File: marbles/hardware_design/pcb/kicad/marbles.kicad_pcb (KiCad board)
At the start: 2 copper layers, 88.9 x 106 mm, 213 parts, among them IC1 R-78E3.3-0.5, IC10 TL074PW, IC2 STM32F405RGT6, IC3 LD2981ABU33, IC4 DAC8164ICPW, IC5 MCP6004, IC6 MCP6004, IC7 OPA4171, IC8 LM4040B10, IC9 LM324PW, J1 PJ301_THONKICONN6, J10 PJ301_THONKICONN6, J11 PJ301_THONKICONN6, J12 PJ301_THONKICONN6, J13 PJ301_THONKICONN6, J14 PJ301_THONKICONN6, J15 PJ301_THONKICONN6, J16 PJ301_THONKICONN6, J2 PJ301_THONKICONN6, J3 PJ301_THONKICONN6, J4 PJ301_THONKICONN6, J5 PJ301_THONKICONN6, J6 PJ301_THONKICONN6, J7 PJ301_THONKICONN6, J8 PJ301_THONKICONN6, J9 PJ301_THONKICONN6, Q1 8MHz, Q2 MMBT3904, Q3 MMBT3904, SW1 LP4OA1PBCT, SW2 LP4OA1PBCT

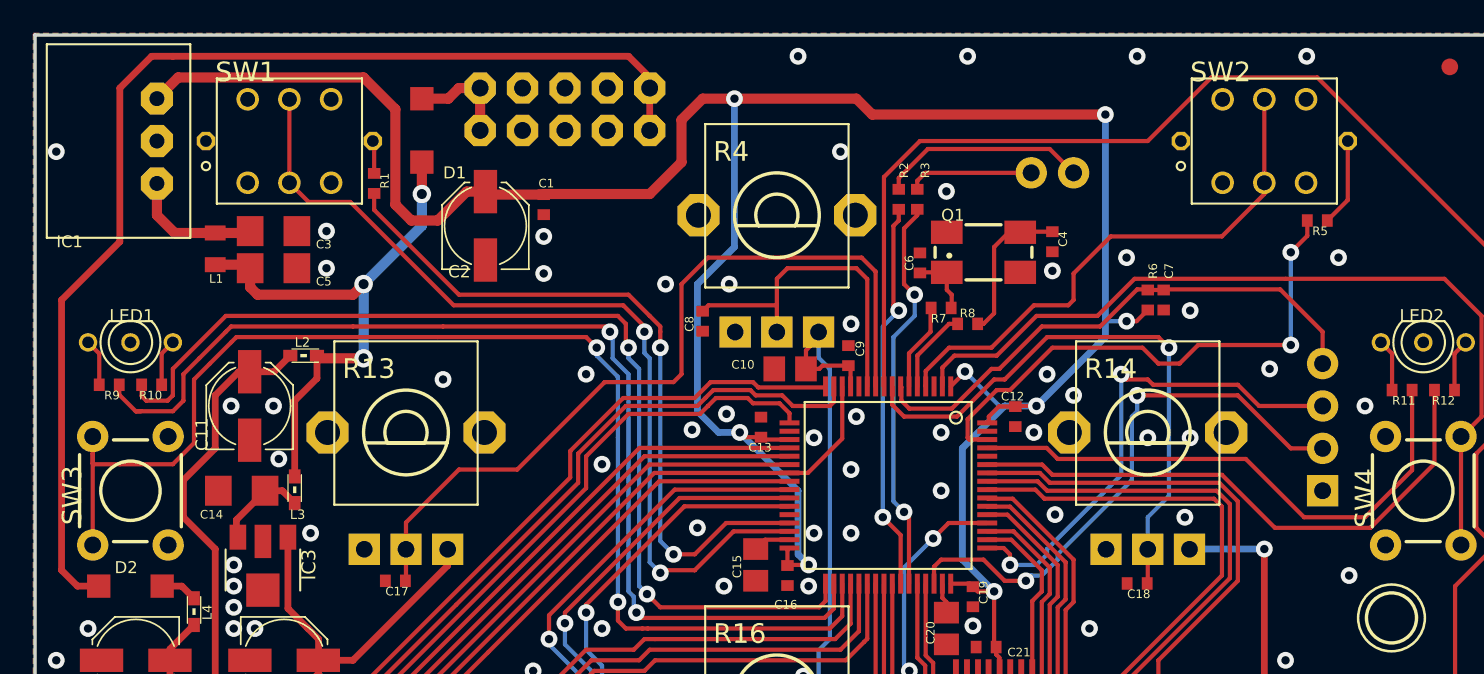
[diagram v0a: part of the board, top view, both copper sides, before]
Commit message: replace led/button switches
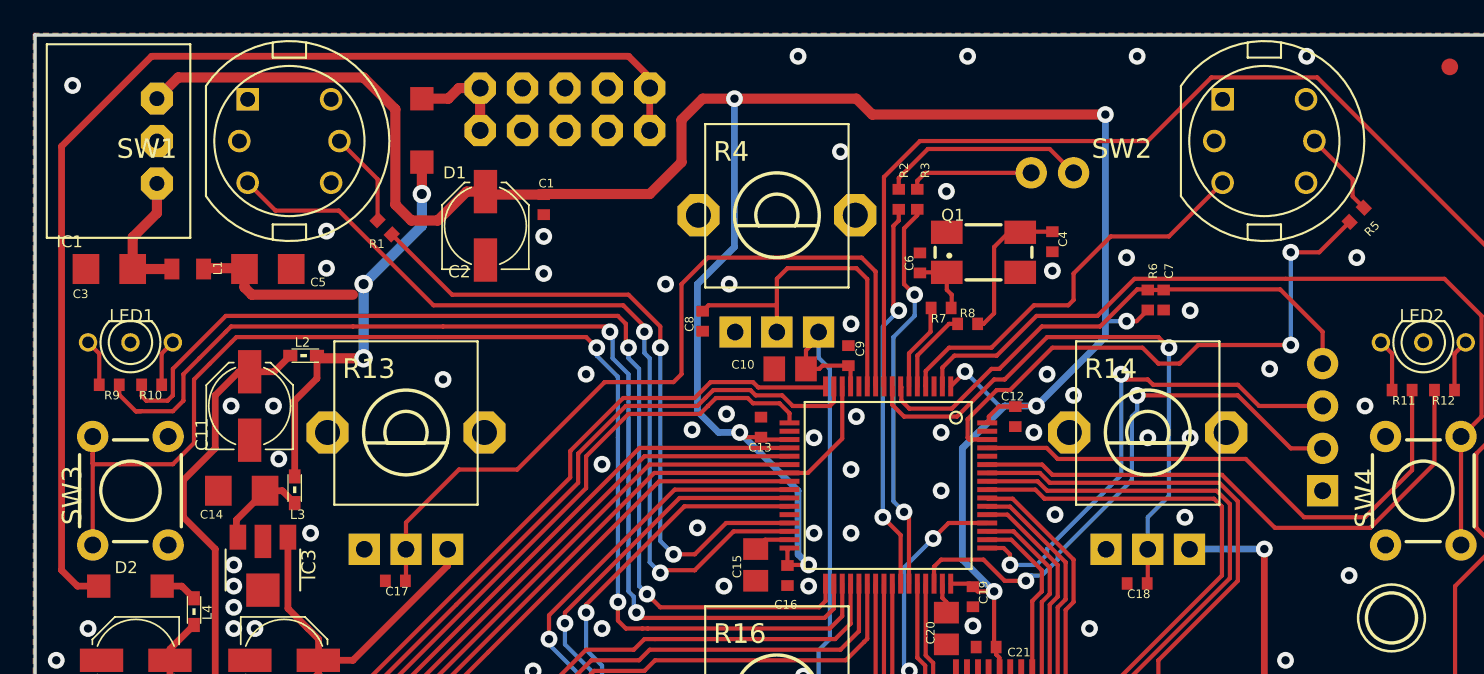
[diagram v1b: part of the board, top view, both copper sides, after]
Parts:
- removed U$2: , marbles:ROHS_BIG
- removed U$4: , marbles:CE_MEDIUM
- removed U$5: , marbles:FCC_MEDIUM
- JP1: value (none) -> M04PTH
- JP2: value (none) -> M02PTH
- L2, L3, L4: value (none) -> WE-CBF_0603
- SW1, SW2: value LP4OA1PBCT -> SW_Push_LED; footprint marbles:LP4OA1PBCT -> Supercell 1.3:C&K_D6R
- SW3, SW4, SW5, SW6, SW7: value (none) -> TAC_SWITCHPTH
- moved C3 10.1 mm to (108.5, 66.0), turned to 180 degrees
- moved R1 2.70 mm to (125.0, 63.5), turned to 135 degrees
- moved R5 2.39 mm to (183.2, 62.8), turned to 45 degrees
- moved L1 1.97 mm to (113.2, 66.0), turned to 180 degrees
- moved C5 0.34 mm to (118.0, 66.0)
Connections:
- net DAC_MOSI renamed /marbles_2/DAC_MOSI
- net DAC_SCK renamed /marbles_2/DAC_SCK
- net DAC_SS renamed /marbles_2/DAC_SS
- net DEPRECATED renamed /marbles_4/DEPRECATED
- net MORPH_IN renamed Net-(C53-Pad1)
- net MORPH_IN1 renamed Net-(C55-Pad1)
- net MORPH_IN3 renamed Net-(C56-Pad1)
- net MORPH_IN4 renamed Net-(C57-Pad1)
- net MORPH_IN5 renamed Net-(C54-Pad1)
- net MORPH_IN6 renamed Net-(C58-Pad1)
- net MORPH_IN7 renamed Net-(C45-Pad1)
- net RESET renamed /marbles_2/RESET
- net RX renamed /marbles_2/RX
- net SWCLK renamed /marbles_2/SWCLK
- net SWDIO renamed /marbles_2/SWDIO
- net TX renamed /marbles_2/TX
- net VREF_BIAS renamed /marbles_5/VREF_BIAS
- IC2 pad 3: (no net) -> unconnected-(IC2-Pad3)
- J10 pad P2: (no net) -> unconnected-(J10-PadP2)
- J11 pad P2: (no net) -> unconnected-(J11-PadP2)
- J12 pad P2: (no net) -> unconnected-(J12-PadP2)
- J13 pad P2: (no net) -> unconnected-(J13-PadP2)
- J14 pad P2: (no net) -> unconnected-(J14-PadP2)
- J15 pad P2: (no net) -> unconnected-(J15-PadP2)
- J16 pad P2: (no net) -> unconnected-(J16-PadP2)
- LED5 pad 3: (no net) -> unconnected-(LED5-Pad3)
- R1 pad 2: N$1 -> Net-(R1-Pad2)
- R5 pad 2: N$2 -> Net-(R5-Pad2)
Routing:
- net SW_X_DV: track 32.2 -> 24.4 mm
- net Net-(R1-Pad2): track 0.00 -> 5.69 mm
- net N$2: track 5.27 -> 0.00 mm
- net Net-(R5-Pad2): track 0.00 -> 5.22 mm
- net LED_T_DV: track 42.7 -> 40.1 mm
- net SW_T_DV: track 53.8 -> 51.3 mm
- net N$1: track 1.97 -> 0.00 mm
- net LED_X_DV: track 32.2 -> 34.2 mm

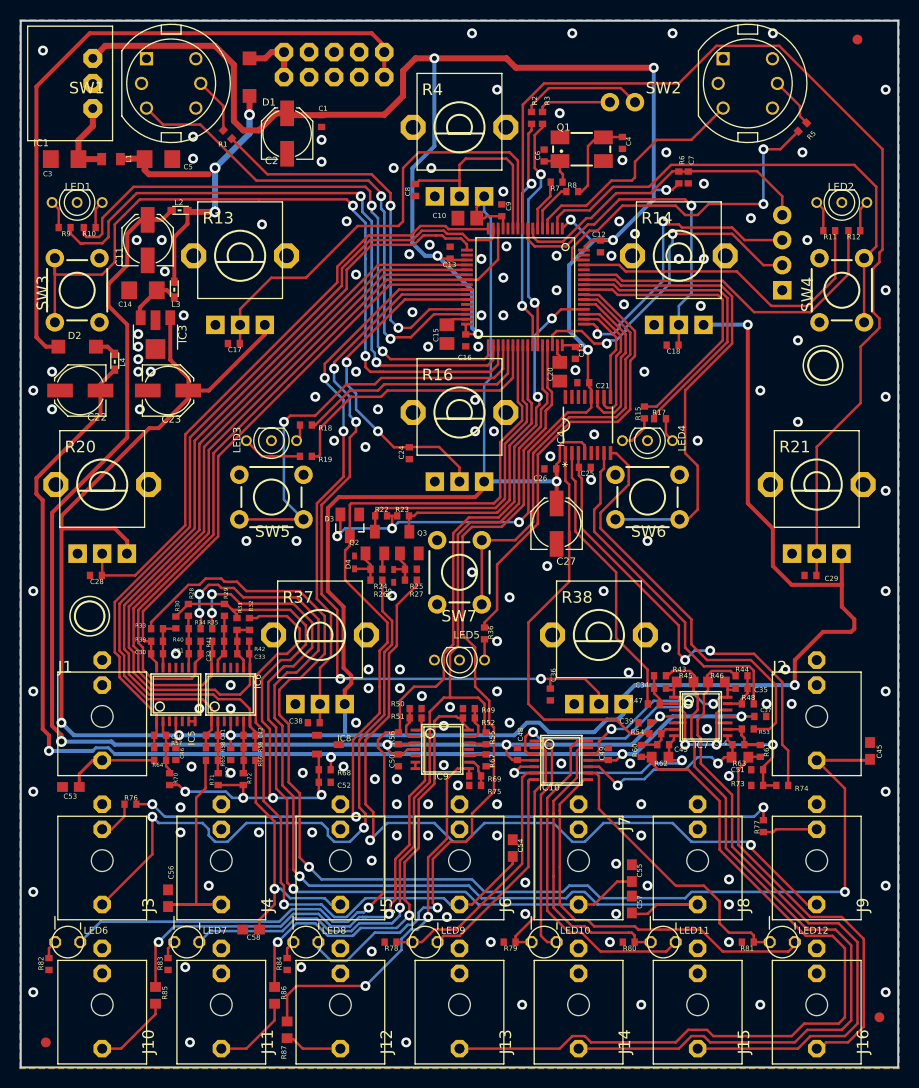
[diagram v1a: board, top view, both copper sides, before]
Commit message: added SMD LEDs in parallel with THT footprint
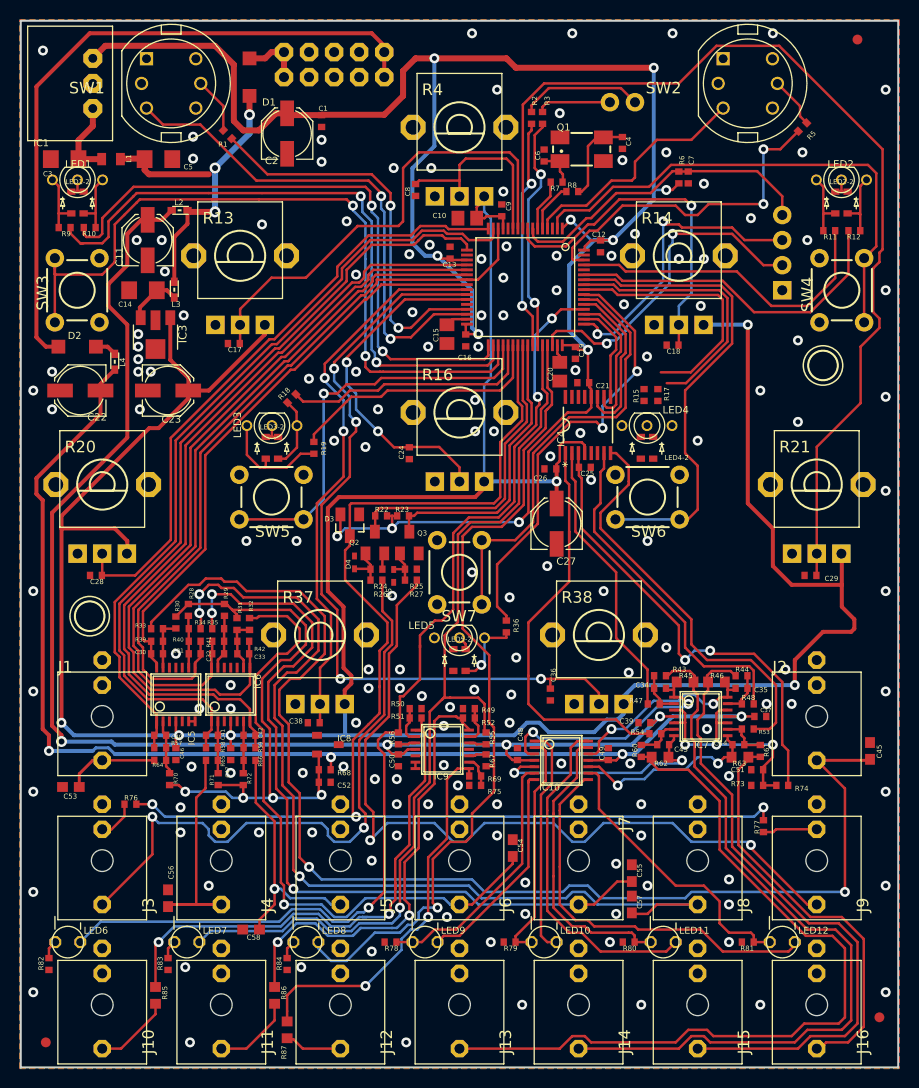
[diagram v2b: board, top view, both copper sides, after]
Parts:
- added LED1-2: LED_Dual_KAKA, Supercell 1.3:bicolor 0606 LED, F.Cu at (109.8, 70.4)
- added LED2-2: LED_Dual_KAKA, Supercell 1.3:bicolor 0606 LED, F.Cu at (187.2, 70.4)
- added LED3-2: LED_Dual_KAKA, Supercell 1.3:bicolor 0606 LED, F.Cu at (129.5, 95.2)
- added LED4-2: LED_Dual_KAKA, Supercell 1.3:bicolor 0606 LED, F.Cu at (167.5, 95.2)
- added LED5-2: LED_Dual_KAKA, Supercell 1.3:bicolor 0606 LED, F.Cu at (148.5, 116.8)
- LED1, LED2, LED3, LED4, LED5: value W115WSURKMGKW -> LED-BICOLOR-THROUGHHOLE
- moved R18 3.05 mm to (131.5, 90.2), turned to -135 degrees
- moved R17 2.41 mm to (168.6, 89.9), turned to -90 degrees
- moved R36 2.32 mm to (153.2, 113.3)
- moved LED2 2.30 mm to (187.2, 68.1)
- moved LED1 2.30 mm to (109.8, 68.1)
- moved LED5 2.25 mm to (148.5, 114.5)
- moved R15 1.77 mm to (167.2, 89.9)
- moved LED4 1.53 mm to (167.5, 93.0)
- moved LED3 1.53 mm to (129.5, 93.0)
- moved R19 1.18 mm to (133.8, 95.2), turned to -90 degrees
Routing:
- net GND: track 1.68 -> 10.5 mm, vias 159 -> 160
- net Net-(LED3-2-PadAR): track 6.09 -> 11.8 mm
- net Net-(LED3-2-PadAG): track 1.73 -> 7.32 mm
- net Net-(LED5-2-PadAG): track 2.10 -> 7.48 mm, vias 0 -> 1
- net Net-(LED4-2-PadAR): track 3.74 -> 0.00 mm
- net Net-(LED2-2-PadAR): track 3.14 -> 6.78 mm
- net Net-(LED2-2-PadAG): track 3.14 -> 6.74 mm
- net Net-(LED1-Pad3): track 2.82 -> 6.38 mm
- net Net-(LED1-2-PadAG): track 2.82 -> 6.35 mm
- net LED_X_RANGE_R: track 29.3 -> 26.2 mm
- net LED_X_RANGE_G: track 30.4 -> 27.4 mm
- net Net-(LED4-2-PadAG): track 2.50 -> 0.00 mm
- net SW_T_RANGE: track 44.0 -> 41.7 mm
- net LED_T_RANGE_R: track 28.6 -> 26.6 mm
- net ADC_T_JITTER_CV: track 79.2 -> 80.3 mm
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
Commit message: bottom row output LEDs to SMD
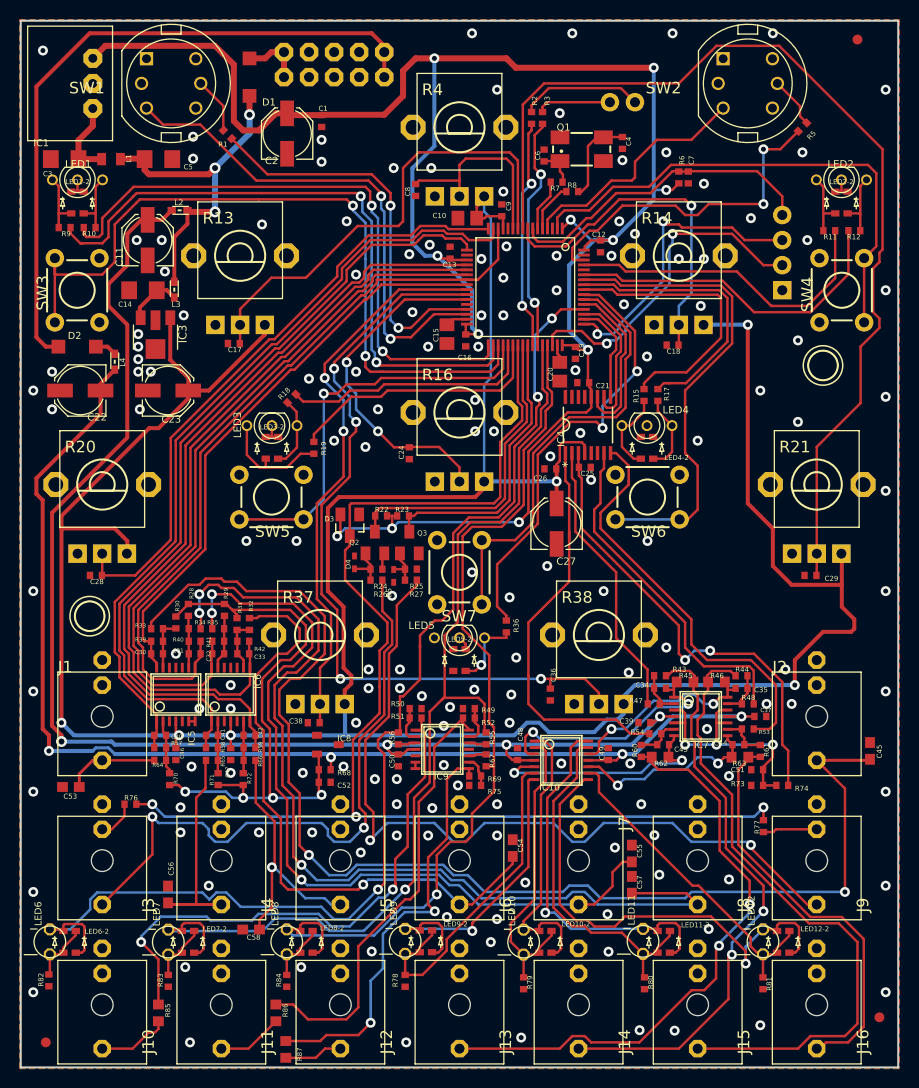
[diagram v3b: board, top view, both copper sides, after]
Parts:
- added LED10-2: LED_Dual_KAKA, Supercell 1.3:bicolor 0606 LED, F.Cu at (157.2, 145.3)
- added LED11-2: LED_Dual_KAKA, Supercell 1.3:bicolor 0606 LED, F.Cu at (169.2, 145.3)
- added LED12-2: LED_Dual_KAKA, Supercell 1.3:bicolor 0606 LED, F.Cu at (181.3, 145.3)
- added LED6-2: LED_Dual_KAKA, Supercell 1.3:bicolor 0606 LED, F.Cu at (109.0, 145.3)
- added LED7-2: LED_Dual_KAKA, Supercell 1.3:bicolor 0606 LED, F.Cu at (121.0, 145.3)
- added LED8-2: LED_Dual_KAKA, Supercell 1.3:bicolor 0606 LED, F.Cu at (133.0, 145.3)
- added LED9-2: LED_Dual_KAKA, Supercell 1.3:bicolor 0606 LED, F.Cu at (145.1, 145.2)
- moved R80 4.47 mm to (167.2, 149.5), turned to -90 degrees
- moved R81 4.45 mm to (179.2, 149.5), turned to -90 degrees
- moved R79 4.41 mm to (155.0, 149.5), turned to -90 degrees
- moved R78 4.20 mm to (143.0, 149.2), turned to -90 degrees
- moved LED10 2.07 mm to (155.0, 145.3), turned to -90 degrees
- moved LED11 2.04 mm to (167.1, 145.2), turned to -90 degrees
- moved LED9 2.01 mm to (143.0, 145.2), turned to -90 degrees
- moved C55 1.99 mm to (166.0, 136.3)
- moved C57 1.99 mm to (166.0, 139.5)
- moved R87 1.99 mm to (130.9, 156.2)
- moved LED12 1.95 mm to (179.2, 145.3), turned to -90 degrees
- moved LED8 1.94 mm to (131.0, 145.3), turned to -90 degrees
- moved LED7 1.88 mm to (119.0, 145.3), turned to -90 degrees
- moved LED6 1.81 mm to (107.0, 145.3), turned to -90 degrees
- moved R85 1.80 mm to (118.0, 152.5)
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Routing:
- net Net-(J13-PadP3): track 80.3 -> 60.3 mm, vias 0 -> 2
- net Net-(J14-PadP3): track 76.4 -> 58.3 mm, vias 0 -> 2
- net GATE_T_1: track 107.3 -> 119.4 mm
- net Net-(IC10-Pad7): track 21.8 -> 33.1 mm, vias 0 -> 1
- net GATE_T_2: track 96.0 -> 105.3 mm
- net Net-(IC10-Pad8): track 40.4 -> 49.1 mm, vias 0 -> 1
- net Net-(LED4-2-PadAR): track 0.00 -> 8.49 mm
- net Net-(LED4-2-PadAG): track 0.00 -> 7.96 mm
- net Net-(IC10-Pad6): track 26.2 -> 33.8 mm
- net GATE_T_3: track 84.3 -> 91.8 mm
- net Net-(IC10-Pad2): track 23.5 -> 30.6 mm
- net Net-(IC10-Pad1): track 23.4 -> 29.7 mm
- net Net-(IC10-Pad13): track 29.8 -> 35.8 mm
- net Net-(LED8-Pad2): track 1.89 -> 6.24 mm
- net Net-(LED6-Pad2): track 1.89 -> 6.23 mm
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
